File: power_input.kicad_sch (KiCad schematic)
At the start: 8 parts, among them J1 DC005-T20, U1 DCDC Converter

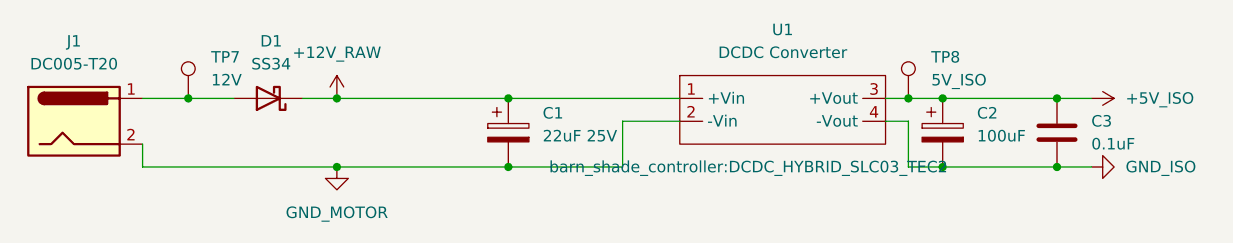
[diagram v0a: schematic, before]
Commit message: Updating routing with new terminal block
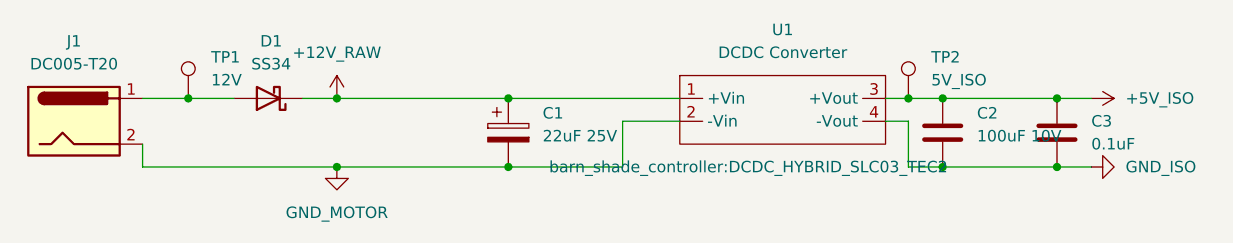
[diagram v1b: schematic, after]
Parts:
- C2: value 100uF -> 100uF 10V; footprint Capacitor_SMD:CP_Elec_6.3x5.4 -> Capacitor_SMD:C_1210_3225Metric; symbol Device:C_Polarized -> Device:C; LCSC C7469977 -> (none)
- TP1: renamed from TP7; footprint barn_shade_controller:TestPoint_Pad_D1.0mm_No_SolderMask -> TestPoint:TestPoint_Pad_D1.0mm
- TP2: renamed from TP8; footprint barn_shade_controller:TestPoint_Pad_D1.0mm_No_SolderMask -> TestPoint:TestPoint_Pad_D1.0mm

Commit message: Update annotations, fixed font sizes.
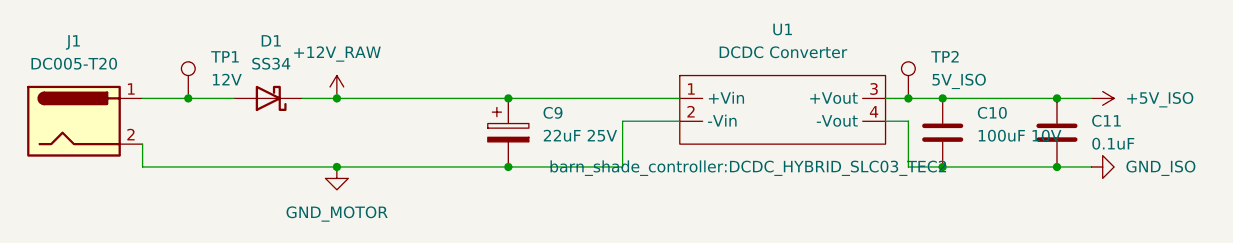
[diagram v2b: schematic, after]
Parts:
- renumbered C2 to C10, C3 to C11, C1 to C9
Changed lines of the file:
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@@
 		(dnp no)
 		(fields_autoplaced yes)
-		(property "Reference" "C1"
+		(property "Reference" "C9"
 			(at 128.27 76.5809 0)
 			(show_name no)
@@
 			(project "barn-blinds-controller"
 				(path "/aa90962a-81b9-423d-8acd-c4e83fa798bb/bb2a80bd-a98d-4040-85a8-f5c2f3802634"
-					(reference "C1")
+					(reference "C9")
 					(unit 1)
 				)
@@
 		(dnp no)
 		(fields_autoplaced yes)
-		(property "Reference" "C3"
+		(property "Reference" "C11"
 			(at 189.23 77.4699 0)
 			(show_name no)
@@
 			(project "barn-blinds-controller"
 				(path "/aa90962a-81b9-423d-8acd-c4e83fa798bb/bb2a80bd-a98d-4040-85a8-f5c2f3802634"
-					(reference "C3")
+					(reference "C11")
 					(unit 1)
 				)
@@
 		(dnp no)
 		(fields_autoplaced yes)
-		(property "Reference" "C2"
+		(property "Reference" "C10"
 			(at 176.53 76.5809 0)
 			(show_name no)
@@
 			(project "barn-blinds-controller"
 				(path "/aa90962a-81b9-423d-8acd-c4e83fa798bb/bb2a80bd-a98d-4040-85a8-f5c2f3802634"
-					(reference "C2")
-					(unit 1)
-				)
+					(reference "C10")
+					(unit 1)
+				)
